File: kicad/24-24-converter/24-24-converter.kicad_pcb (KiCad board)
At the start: 4 copper layers, 143.5 x 76 mm, 79 parts, among them J1 Conn_01x02, J2 Conn_01x02, M1 CSD18540Q5B, M1_1 CSD18540Q5B, M2 CSD18540Q5B, M2_1 CSD18540Q5B, M3 GENERIC_MOSFET_N, M3_1 GENERIC_MOSFET_N, M4 GENERIC_MOSFET_N, U1 LM5176PWPR

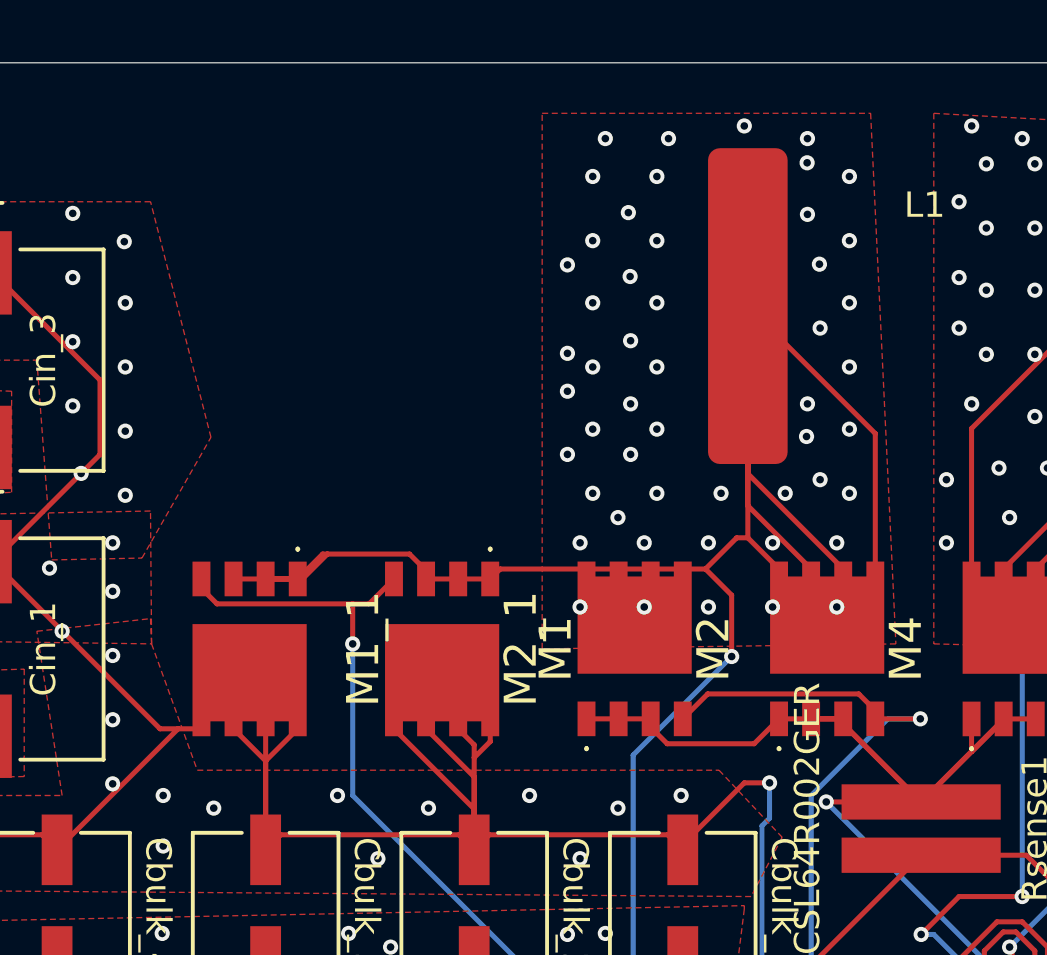
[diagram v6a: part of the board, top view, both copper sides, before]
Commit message: added high current paths to Coutx
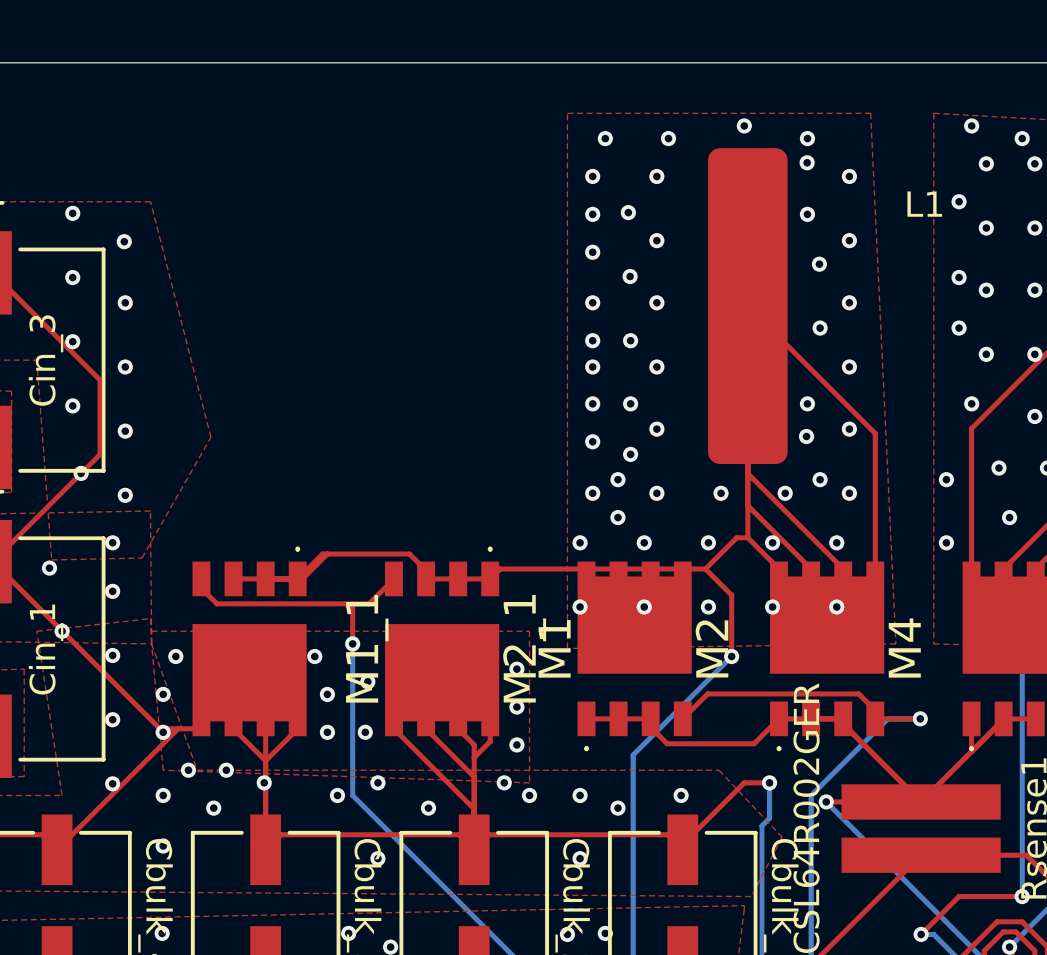
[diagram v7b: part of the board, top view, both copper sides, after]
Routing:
- net VIN: vias 77 -> 94
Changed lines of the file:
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@@
 	)
 	(via
+		(at 124.5 76.5)
+		(size 0.6)
+		(drill 0.3)
+		(layers "F.Cu" "B.Cu")
+		(free yes)
+		(net "VIN")
+	)
+	(via
+		(at 119.5 81)
+		(size 0.6)
+		(drill 0.3)
+		(layers "F.Cu" "B.Cu")
+		(free yes)
+		(net "VIN")
+	)
+	(via
 		(at 110 72)
 		(size 0.6)
@@
 	)
 	(via
+		(at 132 81.5)
+		(size 0.6)
+		(drill 0.3)
+		(layers "F.Cu" "B.Cu")
+		(free yes)
+		(net "VIN")
+	)
+	(via
 		(at 117 62.5)
 		(size 0.6)
@@
 	)
 	(via
+		(at 126.5 79.5)
+		(size 0.6)
+		(drill 0.3)
+		(layers "F.Cu" "B.Cu")
+		(free yes)
+		(net "VIN")
+	)
+	(via
 		(at 103 71.96)
 		(size 0.6)
@@
 	)
 	(via
+		(at 125 79.5)
+		(size 0.6)
+		(drill 0.3)
+		(layers "F.Cu" "B.Cu")
+		(free yes)
+		(net "VIN")
+	)
+	(via
 		(at 80 72.5)
 		(size 0.6)
@@
 	)
 	(via
+		(at 118.5 79.5)
+		(size 0.6)
+		(drill 0.3)
+		(layers "F.Cu" "B.Cu")
+		(free yes)
+		(net "VIN")
+	)
+	(via
+		(at 122.5 81.5)
+		(size 0.6)
+		(drill 0.3)
+		(layers "F.Cu" "B.Cu")
+		(free yes)
+		(net "VIN")
+	)
+	(via
+		(at 127 81.5)
+		(size 0.6)
+		(drill 0.3)
+		(layers "F.Cu" "B.Cu")
+		(free yes)
+		(net "VIN")
+	)
+	(via
 		(at 116.5 79)
 		(size 0.6)
@@
 	)
 	(via
+		(at 121 81)
+		(size 0.6)
+		(drill 0.3)
+		(layers "F.Cu" "B.Cu")
+		(free yes)
+		(net "VIN")
+	)
+	(via
+		(at 132.5 77)
+		(size 0.6)
+		(drill 0.3)
+		(layers "F.Cu" "B.Cu")
+		(free yes)
+		(net "VIN")
+	)
+	(via
 		(at 98.42 60)
 		(size 0.6)
@@
 	)
 	(via
+		(at 125 78)
+		(size 0.6)
+		(drill 0.3)
+		(layers "F.Cu" "B.Cu")
+		(free yes)
+		(net "VIN")
+	)
+	(via
 		(at 93.42 84)
 		(size 0.6)
@@
 	)
 	(via
+		(at 119 76.5)
+		(size 0.6)
+		(drill 0.3)
+		(layers "F.Cu" "B.Cu")
+		(free yes)
+		(net "VIN")
+	)
+	(via
 		(at 127 84.5)
 		(size 0.6)
@@
 	)
 	(via
+		(at 132.5 80)
+		(size 0.6)
+		(drill 0.3)
+		(layers "F.Cu" "B.Cu")
+		(free yes)
+		(net "VIN")
+	)
+	(via
+		(at 118.5 78)
+		(size 0.6)
+		(drill 0.3)
+		(layers "F.Cu" "B.Cu")
+		(free yes)
+		(net "VIN")
+	)
+	(via
 		(at 110 84.5)
 		(size 0.6)
@@
 	)
 	(via
+		(at 126.6 77.5)
+		(size 0.6)
+		(drill 0.3)
+		(layers "F.Cu" "B.Cu")
+		(free yes)
+		(net "VIN")
+	)
+	(via
 		(at 133 82)
 		(size 0.6)
@@
 	)
 	(via
+		(at 132.5 78.5)
+		(size 0.6)
+		(drill 0.3)
+		(layers "F.Cu" "B.Cu")
+		(free yes)
+		(net "VIN")
+	)
+	(via
 		(at 105.92 59.96)
 		(size 0.6)
@@
 	)
 	(via
+		(at 135 82)
+		(size 0.6)
+		(drill 0.3)
+		(layers "F.Cu" "B.Cu")
+		(free yes)
+		(net "VIN")
+	)
+	(via
 		(at 114.5 75.5)
 		(size 0.6)
@@
 	)
 	(via
-		(at 135.5 67.5)
+		(at 135.5 68)
 		(size 0.6)
 		(drill 0.3)
@@
 	)
 	(via
-		(at 134.5 61)
+		(at 135.5 59)
 		(size 0.6)
 		(drill 0.3)
@@
 	)
 	(via
-		(at 135.5 60.04)
+		(at 135.5 60.5)
 		(size 0.6)
 		(drill 0.3)
@@
 	)
 	(via
-		(at 134.5 64.5)
+		(at 135.5 64)
 		(size 0.6)
 		(drill 0.3)
@@
 	)
 	(via
-		(at 134.5 66)
+		(at 135.5 66.5)
 		(size 0.6)
 		(drill 0.3)
@@
 	)
 	(via
-		(at 134.5 68.5)
+		(at 136.5 69.5)
 		(size 0.6)
 		(drill 0.3)
@@
 		(polygon
 			(pts
-				(xy 146.5 55) (xy 147.5 76) (xy 133.5 76.1969) (xy 133.5 55)
+				(xy 146.5 55) (xy 147.5 76) (xy 134.5 76.182836) (xy 134.5 55)
 			)
 		)
@@
 	)
 	(zone
+		(net "VIN")
+		(layer "F.Cu")
+		(hatch edge 0.5)
+		(priority 31)
+		(connect_pads yes
+			(clearance 0.6)
+		)
+		(min_thickness 0.4)
+		(fill yes
+			(thermal_gap 0.5)
+			(thermal_bridge_width 0.5)
+			(smoothing chamfer)
+			(radius 0.75)
+			(island_removal_mode 0)
+		)
+		(polygon
+			(pts
+				(xy 118.040952 75.5) (xy 133 75.5) (xy 133 81.5) (xy 118.5 81) (xy 118.040952 75.99925)
+			)
+		)
+	)
+	(zone
 		(net "VOUT")
 		(layer "F.Cu")
@@
 	)
 	(zone
+		(net "VIN")
+		(layer "In1.Cu")
+		(hatch edge 0.5)
+		(priority 32)
+		(connect_pads yes
+			(clearance 0.6)
+		)
+		(min_thickness 0.4)
+		(fill yes
+			(thermal_gap 0.5)
+			(thermal_bridge_width 0.5)
+			(smoothing chamfer)
+			(radius 0.75)
+			(island_removal_mode 0)
+		)
+		(polygon
+			(pts
+				(xy 118 75.5) (xy 133 75.5) (xy 133 81.5) (xy 120 81.5)
+			)
+		)
+	)
+	(zone
 		(net "GND")
 		(layer "In1.Cu")
@@
 		(polygon
 			(pts
-				(xy 146.5 55) (xy 147.5 76.5) (xy 133.5 76.5) (xy 133.5 55)
+				(xy 146.5 55) (xy 147.5 76.5) (xy 134.5 76.5) (xy 134.5 55)
 			)
 		)
